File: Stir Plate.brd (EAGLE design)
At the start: 38 x 38 mm, 18 parts, among them IC1 555NEN, Q1 TIP31

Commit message: Correct Pot footprint / library entry
TODO: Fix board
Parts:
- R3: device Stir Plate:RJ9W -> Stir Plate:3RP/1610N
- moved R3 173.8 mm to (-9.50, 13.0), turned to 0 degrees
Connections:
- net N$10: now also R3.3; no longer R3.S
- net N$4: now also R3.2; no longer R3.E
- net N$5: now also R3.1; no longer R3.A
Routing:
- net GND: track 79.9 -> 57.8 mm
- net N$10: track 15.5 -> 0.00 mm
- net N$3: track 17.4 -> 3.96 mm
- net N$5: track 12.4 -> 0.00 mm
- net N$4: track 10.9 -> 0.00 mm
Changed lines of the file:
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@@
 <layer number="220" name="220bmp" color="21" fill="1" visible="no" active="no"/>
 <layer number="221" name="221bmp" color="22" fill="1" visible="no" active="no"/>
+<layer number="222" name="222bmp" color="23" fill="1" visible="no" active="no"/>
 <layer number="223" name="223bmp" color="24" fill="1" visible="no" active="no"/>
 <layer number="224" name="224bmp" color="25" fill="1" visible="no" active="no"/>
@@
 <attribute name="NAME" x="126.036" y="99.642" size="1.27" layer="25" ratio="10" rot="R90"/>
 </element>
-<element name="R3" library="Stir Plate" package="RJ9W" value="10kR" x="146.09" y="90.355" smashed="yes" rot="R180">
-<attribute name="NAME" x="151.297" y="92.387" size="1.27" layer="25" ratio="10" rot="R270"/>
-</element>
 <element name="C1" library="Stir Plate" package="C025-030X050" value="0.0047uF" x="132.64" y="91.26" smashed="yes" rot="R90">
 <attribute name="NAME" x="130.735" y="88.974" size="1.27" layer="25" ratio="10" rot="R90"/>
@@
 <element name="FRAME1" library="Stir Plate" package="FRAME_A_L" value="" x="0" y="0"/>
 <element name="U$1" library="Stir Plate" package="DOCFIELD" value="DOCFIELD" x="172.22" y="-0.03"/>
+<element name="R3" library="Stir Plate" package="3RP/1610N" value="10kR" x="-9.5" y="13"/>
 </elements>
 <signals>
@@
 <wire x1="134.98" y1="90.18" x2="136.26" y2="90.18" width="0.6096" layer="16"/>
 <wire x1="136.26" y1="90.18" x2="136.45" y2="89.99" width="0.6096" layer="16"/>
-<wire x1="136.45" y1="89.99" x2="137.29" y2="89.99" width="0.6096" layer="16"/>
-<wire x1="137.29" y1="89.99" x2="141.48" y2="94.18" width="0.6096" layer="16"/>
-<wire x1="141.48" y1="94.18" x2="153.04" y2="94.18" width="0.6096" layer="16"/>
-<wire x1="153.04" y1="94.18" x2="155.725" y2="96.865" width="0.6096" layer="16"/>
 <polygon width="0.4064" layer="16">
 <vertex x="124.5" y="88"/>
@@
 <vertex x="124.5" y="102.5"/>
 </polygon>
+<wire x1="136.45" y1="89.99" x2="155.725" y2="96.865" width="0" layer="19" extent="1-1"/>
 </signal>
 <signal name="N$2">
@@
 <contactref element="R1" pad="1"/>
 <contactref element="D3" pad="C"/>
-<wire x1="150.72" y1="96.475" x2="150.72" y2="100.095" width="0.6096" layer="1"/>
-<wire x1="150.72" y1="100.095" x2="150.625" y2="100.19" width="0.6096" layer="1"/>
 <wire x1="139.625" y1="102.69" x2="140.895" y2="102.69" width="0.6096" layer="1"/>
 <wire x1="140.895" y1="102.69" x2="142.8" y2="104.595" width="0.6096" layer="1"/>
-<wire x1="150.625" y1="100.19" x2="147.205" y2="100.19" width="0.6096" layer="1"/>
-<wire x1="147.205" y1="100.19" x2="142.8" y2="104.595" width="0.6096" layer="1"/>
+<wire x1="150.625" y1="100.19" x2="147.205" y2="100.19" width="0" layer="19" extent="1-16"/>
+<wire x1="147.205" y1="100.19" x2="142.8" y2="104.595" width="0" layer="19" extent="1-16"/>
+<wire x1="150.625" y1="100.19" x2="150.72" y2="96.475" width="0" layer="19" extent="1-1"/>
 </signal>
 <signal name="N$4">
 <contactref element="D3" pad="A"/>
-<contactref element="R3" pad="E"/>
-<wire x1="143.1" y1="96.475" x2="146.185" y2="96.475" width="0.6096" layer="1"/>
-<wire x1="146.185" y1="96.475" x2="148.48" y2="94.18" width="0.6096" layer="1"/>
-<wire x1="148.48" y1="94.18" x2="148.48" y2="89.87" width="0.6096" layer="1"/>
-<wire x1="148.48" y1="89.87" x2="148.63" y2="89.72" width="0.6096" layer="1"/>
+<contactref element="R3" pad="2"/>
+<wire x1="-9.5" y1="13" x2="143.1" y2="96.475" width="0" layer="19" extent="1-1"/>
 </signal>
 <signal name="N$5">
 <contactref element="D2" pad="C"/>
-<contactref element="R3" pad="A"/>
-<wire x1="143.005" y1="100.19" x2="140.98" y2="98.165" width="0.6096" layer="1"/>
-<wire x1="140.98" y1="98.165" x2="140.98" y2="93.18" width="0.6096" layer="1"/>
-<wire x1="140.98" y1="93.18" x2="143.55" y2="90.61" width="0.6096" layer="1"/>
-<wire x1="143.55" y1="90.61" x2="143.55" y2="89.72" width="0.6096" layer="1"/>
+<contactref element="R3" pad="1"/>
+<wire x1="-14.5" y1="13" x2="143.005" y2="100.19" width="0" layer="19" extent="1-1"/>
 </signal>
 <signal name="N$6">
@@
 </signal>
 <signal name="N$10">
-<contactref element="R3" pad="S"/>
 <contactref element="C1" pad="1"/>
-<wire x1="132.64" y1="89.99" x2="134.95" y2="87.68" width="0.6096" layer="1"/>
-<wire x1="134.95" y1="87.68" x2="134.98" y2="87.68" width="0.6096" layer="1"/>
-<wire x1="134.98" y1="87.68" x2="144.48" y2="87.68" width="0.6096" layer="1"/>
-<wire x1="144.48" y1="87.68" x2="146.09" y2="89.29" width="0.6096" layer="1"/>
-<wire x1="146.09" y1="89.29" x2="146.09" y2="89.72" width="0.6096" layer="1"/>
+<contactref element="R3" pad="3"/>
+<wire x1="-4.5" y1="13" x2="132.64" y2="89.99" width="0" layer="19" extent="1-1"/>
 </signal>
 <signal name="N$11">

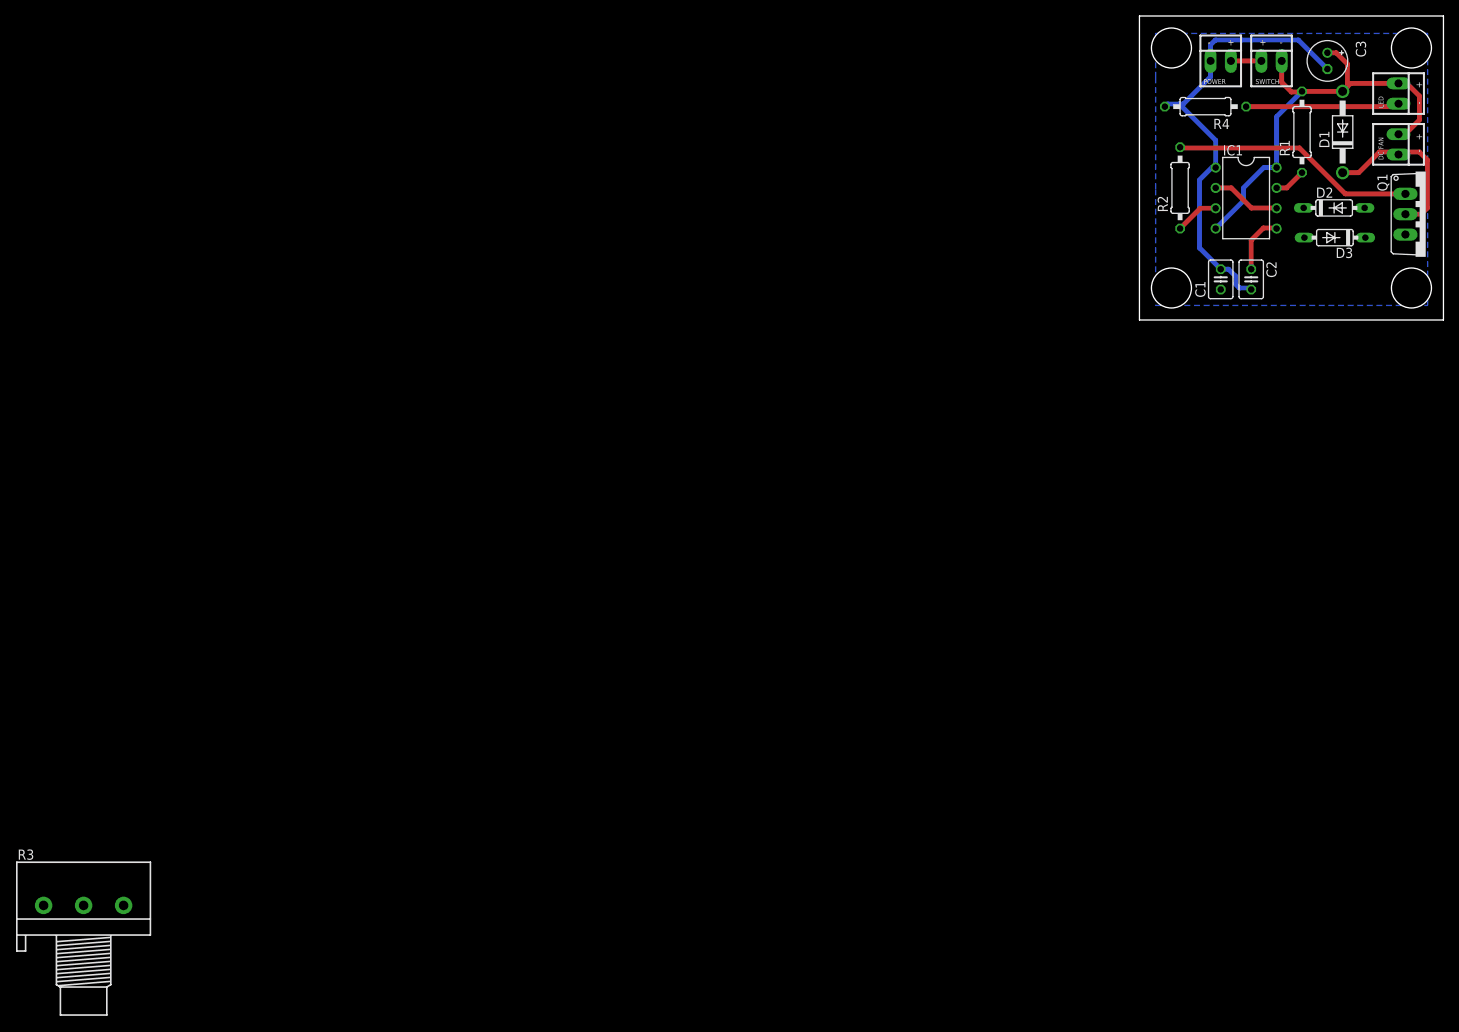
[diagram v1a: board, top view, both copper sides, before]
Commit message: Fixed board layout
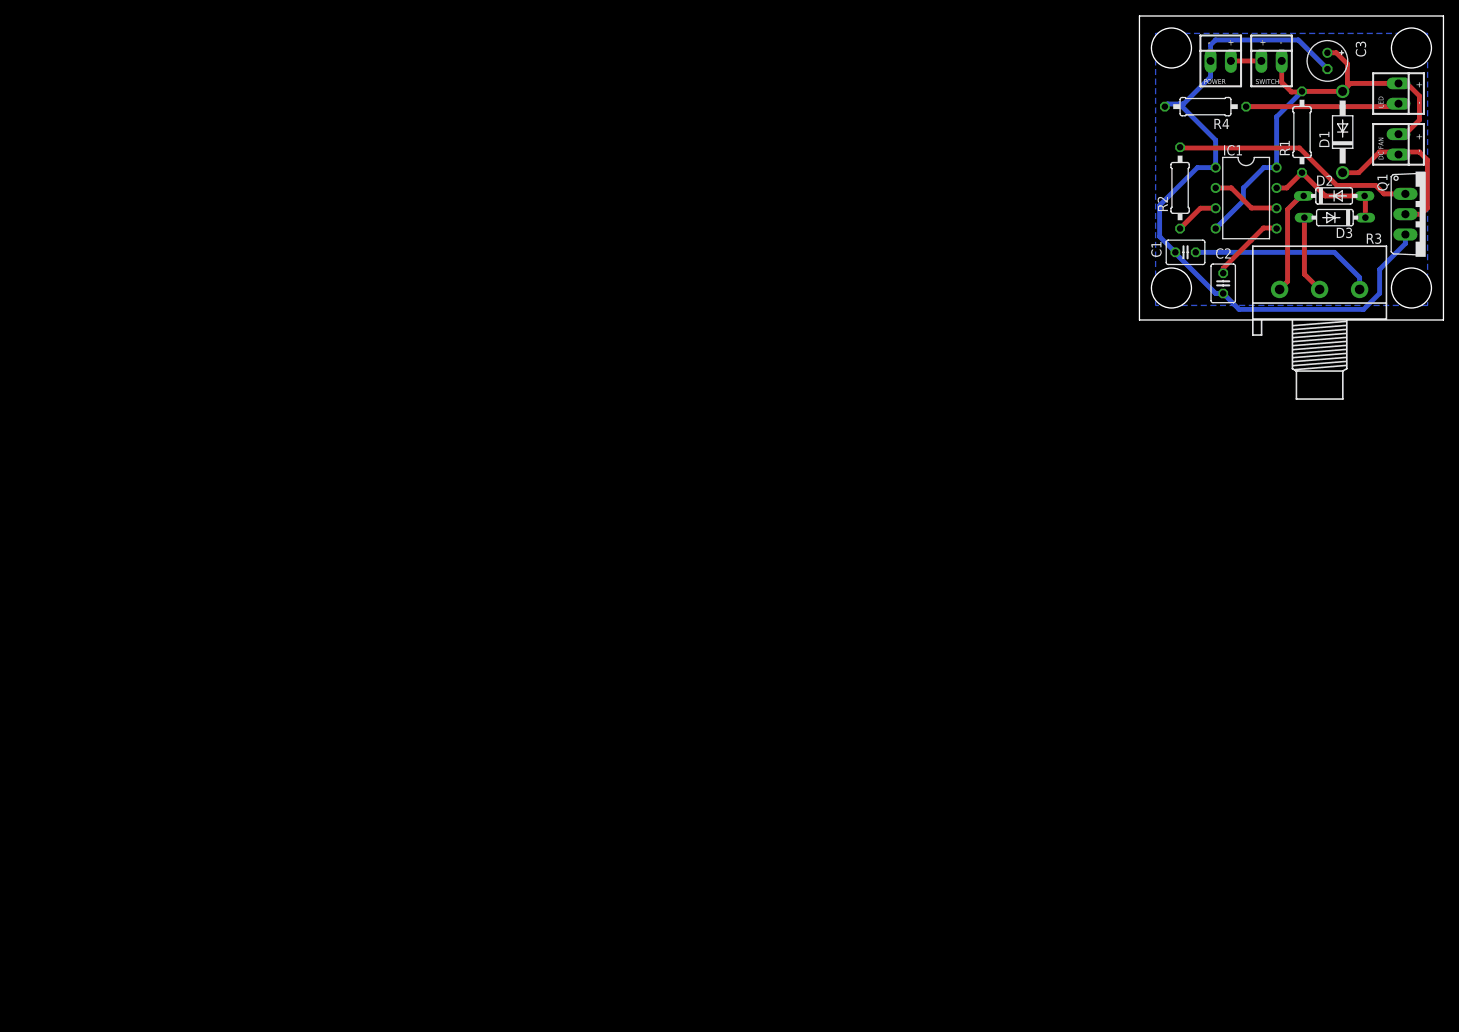
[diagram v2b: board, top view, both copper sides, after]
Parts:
- moved R3 172.6 mm to (145.0, 90.0)
- moved C1 5.55 mm to (128.2, 94.6), turned to 180 degrees
- moved C2 3.54 mm to (132.9, 90.8)
- moved D3 2.50 mm to (146.9, 99.0)
- moved D2 1.50 mm to (146.8, 101.7)
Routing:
- net GND: track 57.8 -> 91.2 mm
- net N$10: track 0.00 -> 23.3 mm
- net N$5: track 0.00 -> 13.1 mm
- net N$3: track 3.96 -> 15.7 mm
- net N$4: track 0.00 -> 9.76 mm
- net N$7: track 7.46 -> 9.41 mm
